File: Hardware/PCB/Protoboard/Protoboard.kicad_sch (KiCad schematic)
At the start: 17 parts, among them J1 Conn_01x05_Female, J2 Conn_01x08_Female, J3 Conn_01x08_Female, U1 MAX6971ANG_

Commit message: Protoboard layout.
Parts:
- R5, R6, R7, R8: value 10 -> 100
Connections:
- net LATCH: now also R1.2; no longer R2.2
- net SCK: now also R2.2; no longer R1.2
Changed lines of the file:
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@@
   (junction (at 165.1 53.34) (diameter 0) (color 0 0 0 0)
   )
-  (junction (at 140.97 26.035) (diameter 0) (color 0 0 0 0)
+  (junction (at 141.605 26.035) (diameter 0) (color 0 0 0 0)
   )
   (junction (at 161.29 50.8) (diameter 0) (color 0 0 0 0)
@@
   )
   (no_connect (at 110.49 45.72))
-  (wire (pts (xy 140.97 22.225) (xy 140.97 26.035))
+  (wire (pts (xy 141.605 22.225) (xy 141.605 26.035))
     (stroke (width 0) (type default) (color 0 0 0 0))
   )
@@
     (stroke (width 0) (type default) (color 0 0 0 0))
   )
+  (wire (pts (xy 142.24 88.9) (xy 140.97 88.9))
+    (stroke (width 0) (type default) (color 0 0 0 0))
+  )
   (wire (pts (xy 153.67 30.48) (xy 157.48 30.48))
     (stroke (width 0) (type default) (color 0 0 0 0))
@@
     (stroke (width 0) (type default) (color 0 0 0 0))
   )
-  (wire (pts (xy 140.97 26.035) (xy 140.97 35.56))
+  (wire (pts (xy 141.605 26.035) (xy 141.605 35.56))
     (stroke (width 0) (type default) (color 0 0 0 0))
   )
@@
     (stroke (width 0) (type default) (color 0 0 0 0))
   )
+  (wire (pts (xy 141.605 26.035) (xy 140.97 26.035))
+    (stroke (width 0) (type default) (color 0 0 0 0))
+  )
   (wire (pts (xy 151.13 66.04) (xy 140.97 66.04))
     (stroke (width 0) (type default) (color 0 0 0 0))
@@
     (stroke (width 0) (type default) (color 0 0 0 0))
   )
+  (wire (pts (xy 141.605 35.56) (xy 140.97 35.56))
+    (stroke (width 0) (type default) (color 0 0 0 0))
+  )
   (wire (pts (xy 168.91 55.88) (xy 140.97 55.88))
     (stroke (width 0) (type default) (color 0 0 0 0))
@@
     (effects (font (size 1.27 1.27)) (justify left bottom))
   )
-  (label "LATCH" (at 55.88 43.18 0)
-    (effects (font (size 1.27 1.27)) (justify left bottom))
-  )
-  (label "SPI1_MOSI" (at 55.88 40.64 0)
-    (effects (font (size 1.27 1.27)) (justify left bottom))
-  )
-  (label "SPI1_5V" (at 55.88 38.1 0)
-    (effects (font (size 1.27 1.27)) (justify left bottom))
-  )
-  (label "SPI1_GND" (at 55.88 48.26 0)
-    (effects (font (size 1.27 1.27)) (justify left bottom))
-  )
-  (label "SPI1_SCK" (at 59.055 45.72 0)
-    (effects (font (size 1.27 1.27)) (justify left bottom))
-  )
-  (global_label "SCK" (shape input) (at 73.66 45.72 0) (fields_autoplaced)
-    (effects (font (size 1.27 1.27)) (justify left))
-    (property "Intersheet References" "${INTERSHEET_REFS}" (id 0) (at 79.8226 45.6406 0)
+  (label "SCK" (at 55.88 43.18 0)
+    (effects (font (size 1.27 1.27)) (justify left bottom))
+  )
+  (label "MOSI" (at 55.88 40.64 0)
+    (effects (font (size 1.27 1.27)) (justify left bottom))
+  )
+  (label "VCC" (at 55.88 38.1 0)
+    (effects (font (size 1.27 1.27)) (justify left bottom))
+  )
+  (label "GND" (at 55.88 48.26 0)
+    (effects (font (size 1.27 1.27)) (justify left bottom))
+  )
+  (label "LATCH" (at 59.055 45.72 0)
+    (effects (font (size 1.27 1.27)) (justify left bottom))
+  )
+  (global_label "LATCH" (shape input) (at 73.66 45.72 0) (fields_autoplaced)
+    (effects (font (size 1.27 1.27)) (justify left))
+    (property "Intersheet References" "${INTERSHEET_REFS}" (id 0) (at 81.7579 45.6406 0)
       (effects (font (size 1.27 1.27)) (justify left) hide)
     )
@@
     )
   )
-  (global_label "LATCH" (shape input) (at 67.31 43.18 0) (fields_autoplaced)
-    (effects (font (size 1.27 1.27)) (justify left))
-    (property "Intersheet References" "${INTERSHEET_REFS}" (id 0) (at 75.4079 43.1006 0)
+  (global_label "SCK" (shape input) (at 67.31 43.18 0) (fields_autoplaced)
+    (effects (font (size 1.27 1.27)) (justify left))
+    (property "Intersheet References" "${INTERSHEET_REFS}" (id 0) (at 73.4726 43.1006 0)
       (effects (font (size 1.27 1.27)) (justify left) hide)
     )
@@
     )
   )
-  (global_label "GND" (shape input) (at 140.97 88.9 0) (fields_autoplaced)
-    (effects (font (size 1.27 1.27)) (justify left))
-    (property "Intersheet References" "${INTERSHEET_REFS}" (id 0) (at 147.2536 88.8206 0)
+  (global_label "GND" (shape input) (at 142.24 88.9 0) (fields_autoplaced)
+    (effects (font (size 1.27 1.27)) (justify left))
+    (property "Intersheet References" "${INTERSHEET_REFS}" (id 0) (at 148.5236 88.8206 0)
       (effects (font (size 1.27 1.27)) (justify left) hide)
     )
@@
     )
   )
-  (global_label "VCC" (shape input) (at 140.97 22.225 90) (fields_autoplaced)
-    (effects (font (size 1.27 1.27)) (justify left))
-    (property "Intersheet References" "${INTERSHEET_REFS}" (id 0) (at 140.8906 16.1833 90)
+  (global_label "VCC" (shape input) (at 141.605 22.225 90) (fields_autoplaced)
+    (effects (font (size 1.27 1.27)) (justify left))
+    (property "Intersheet References" "${INTERSHEET_REFS}" (id 0) (at 141.5256 16.1833 90)
       (effects (font (size 1.27 1.27)) (justify left) hide)
     )
@@
       (effects (font (size 1.27 1.27)) (justify left))
     )
-    (property "Value" "10" (id 1) (at 152.4 29.21 0)
+    (property "Value" "100" (id 1) (at 152.4 29.21 0)
       (effects (font (size 1.27 1.27)) (justify left))
     )
@@
       (effects (font (size 1.27 1.27)) (justify left))
     )
-    (property "Value" "10" (id 1) (at 148.59 29.21 0)
+    (property "Value" "100" (id 1) (at 148.59 29.21 0)
       (effects (font (size 1.27 1.27)) (justify left))
     )
@@
       (effects (font (size 1.27 1.27)) (justify left))
     )
-    (property "Value" "10" (id 1) (at 156.21 29.21 0)
+    (property "Value" "100" (id 1) (at 156.21 29.21 0)
       (effects (font (size 1.27 1.27)) (justify left))
     )
@@
       (effects (font (size 1.27 1.27)) (justify left))
     )
-    (property "Value" "10" (id 1) (at 144.78 29.21 0)
+    (property "Value" "100" (id 1) (at 144.78 29.21 0)
       (effects (font (size 1.27 1.27)) (justify left))
     )
@@
     )
     (path "/de5ce3a4-6348-4028-bcbc-796d25ddc390"
-      (reference "R5") (unit 1) (value "10") (footprint "Resistor_SMD:R_0805_2012Metric_Pad1.20x1.40mm_HandSolder")
+      (reference "R5") (unit 1) (value "100") (footprint "Resistor_SMD:R_0805_2012Metric_Pad1.20x1.40mm_HandSolder")
     )
     (path "/2f1e73e5-ba84-4857-a21b-a2e8a5ea274f"
-      (reference "R6") (unit 1) (value "10") (footprint "Resistor_SMD:R_0805_2012Metric_Pad1.20x1.40mm_HandSolder")
+      (reference "R6") (unit 1) (value "100") (footprint "Resistor_SMD:R_0805_2012Metric_Pad1.20x1.40mm_HandSolder")
     )
     (path "/10f6fcf9-ce65-45e1-81f4-5a5c35568bfc"
-      (reference "R7") (unit 1) (value "10") (footprint "Resistor_SMD:R_0805_2012Metric_Pad1.20x1.40mm_HandSolder")
+      (reference "R7") (unit 1) (value "100") (footprint "Resistor_SMD:R_0805_2012Metric_Pad1.20x1.40mm_HandSolder")
     )
     (path "/60a63df7-538f-43ef-b8d3-5286e6518d70"
-      (reference "R8") (unit 1) (value "10") (footprint "Resistor_SMD:R_0805_2012Metric_Pad1.20x1.40mm_HandSolder")
+      (reference "R8") (unit 1) (value "100") (footprint "Resistor_SMD:R_0805_2012Metric_Pad1.20x1.40mm_HandSolder")
     )
     (path "/3de5d5fd-cc44-4147-a2dc-e5797db63fd1"

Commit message: Finished Protoboard
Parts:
- added H1, H2, H3, H4: MountingHole, MountingHole:MountingHole_2.2mm_M2, symbol Mechanical:MountingHole
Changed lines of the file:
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@@
+    )
+  )
+  (symbol (lib_id "Mechanical:MountingHole") (at 37.465 72.39 0) (unit 1)
+    (in_bom yes) (on_board yes) (fields_autoplaced)
+    (property "Reference" "H3" (id 0) (at 40.64 71.1199 0)
+      (effects (font (size 1.27 1.27)) (justify left))
+    )
+    (property "Value" "MountingHole" (id 1) (at 40.64 73.6599 0)
+      (effects (font (size 1.27 1.27)) (justify left))
+    )
+    (property "Footprint" "MountingHole:MountingHole_2.2mm_M2" (id 2) (at 37.465 72.39 0)
+      (effects (font (size 1.27 1.27)) hide)
+    )
+    (property "Datasheet" "~" (id 3) (at 37.465 72.39 0)
+      (effects (font (size 1.27 1.27)) hide)
     )
   )
@@
     (pin "1")
     (pin "2")
+  )
+  (symbol (lib_id "Mechanical:MountingHole") (at 37.465 77.47 0) (unit 1)
+    (in_bom yes) (on_board yes) (fields_autoplaced)
+    (property "Reference" "H4" (id 0) (at 40.64 76.1999 0)
+      (effects (font (size 1.27 1.27)) (justify left))
+    )
+    (property "Value" "MountingHole" (id 1) (at 40.64 78.7399 0)
+      (effects (font (size 1.27 1.27)) (justify left))
+    )
+    (property "Footprint" "MountingHole:MountingHole_2.2mm_M2" (id 2) (at 37.465 77.47 0)
+      (effects (font (size 1.27 1.27)) hide)
+    )
+    (property "Datasheet" "~" (id 3) (at 37.465 77.47 0)
+      (effects (font (size 1.27 1.27)) hide)
+    )
+  )
+  (symbol (lib_id "Mechanical:MountingHole") (at 37.465 67.31 0) (unit 1)
+    (in_bom yes) (on_board yes) (fields_autoplaced)
+    (property "Reference" "H2" (id 0) (at 40.64 66.0399 0)
+      (effects (font (size 1.27 1.27)) (justify left))
+    )
+    (property "Value" "MountingHole" (id 1) (at 40.64 68.5799 0)
+      (effects (font (size 1.27 1.27)) (justify left))
+    )
+    (property "Footprint" "MountingHole:MountingHole_2.2mm_M2" (id 2) (at 37.465 67.31 0)
+      (effects (font (size 1.27 1.27)) hide)
+    )
+    (property "Datasheet" "~" (id 3) (at 37.465 67.31 0)
+      (effects (font (size 1.27 1.27)) hide)
+    )
   )
   (symbol (lib_id "Device:C") (at 137.16 26.035 90) (unit 1)
@@
     (pin "9")
   )
+  (symbol (lib_id "Mechanical:MountingHole") (at 37.465 62.23 0) (unit 1)
+    (in_bom yes) (on_board yes) (fields_autoplaced)
+    (property "Reference" "H1" (id 0) (at 40.64 60.9599 0)
+      (effects (font (size 1.27 1.27)) (justify left))
+    )
+    (property "Value" "MountingHole" (id 1) (at 40.64 63.4999 0)
+      (effects (font (size 1.27 1.27)) (justify left))
+    )
+    (property "Footprint" "MountingHole:MountingHole_2.2mm_M2" (id 2) (at 37.465 62.23 0)
+      (effects (font (size 1.27 1.27)) hide)
+    )
+    (property "Datasheet" "~" (id 3) (at 37.465 62.23 0)
+      (effects (font (size 1.27 1.27)) hide)
+    )
+  )
   (symbol (lib_id "Device:R") (at 146.05 34.29 0) (unit 1)
     (in_bom yes) (on_board yes)
@@
       (reference "C1") (unit 1) (value "0.1uf") (footprint "Capacitor_SMD:C_0805_2012Metric_Pad1.18x1.45mm_HandSolder")
     )
+    (path "/bfdbfa5d-af60-4bcb-aaee-563dc6121e2f"
+      (reference "H1") (unit 1) (value "MountingHole") (footprint "MountingHole:MountingHole_2.2mm_M2")
+    )
+    (path "/6a9026f4-97ad-4ca6-b8a7-4b78e7eaa11b"
+      (reference "H2") (unit 1) (value "MountingHole") (footprint "MountingHole:MountingHole_2.2mm_M2")
+    )
+    (path "/0d0a8cf0-7e30-4463-a75a-b09ac9dce329"
+      (reference "H3") (unit 1) (value "MountingHole") (footprint "MountingHole:MountingHole_2.2mm_M2")
+    )
+    (path "/683869c3-2652-4a1a-8cb4-4298fc933778"
+      (reference "H4") (unit 1) (value "MountingHole") (footprint "MountingHole:MountingHole_2.2mm_M2")
+    )
     (path "/61c1ad0a-88fa-4e84-b6d4-f39d3cd9072a"

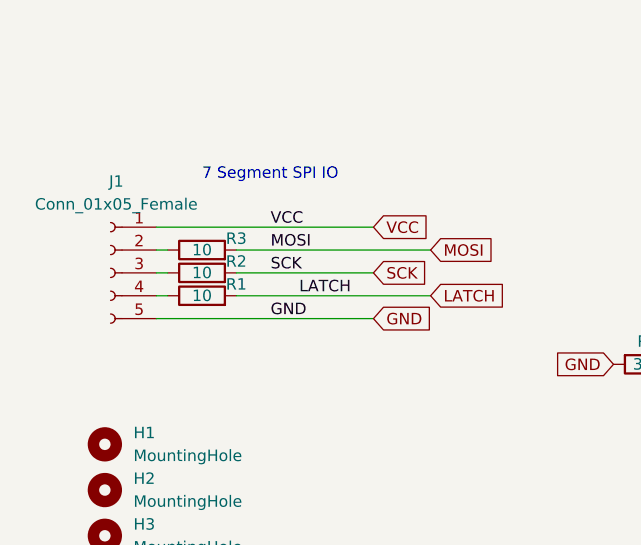
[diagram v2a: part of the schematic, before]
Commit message: Fixed Silkscreen
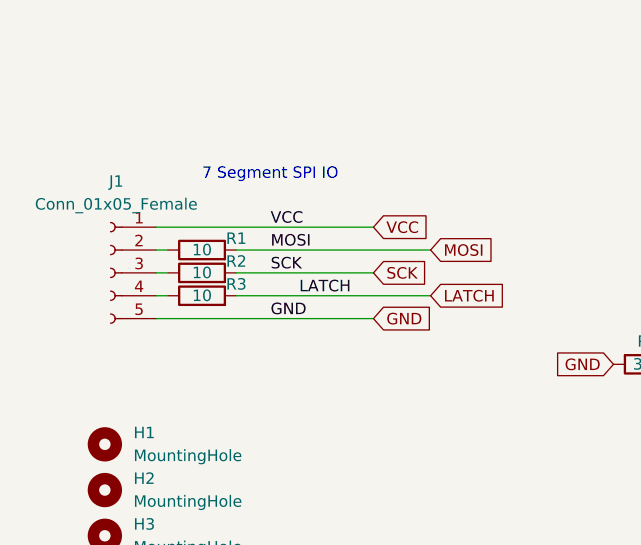
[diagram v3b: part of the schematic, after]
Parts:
- renumbered R3 to R1, R1 to R3
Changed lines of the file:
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@@
   (symbol (lib_id "Device:R") (at 48.26 45.72 90) (unit 1)
     (in_bom yes) (on_board yes)
-    (property "Reference" "R1" (id 0) (at 52.07 44.45 90))
+    (property "Reference" "R3" (id 0) (at 52.07 44.45 90))
     (property "Value" "10" (id 1) (at 48.26 45.72 90))
     (property "Footprint" "Resistor_SMD:R_0805_2012Metric_Pad1.20x1.40mm_HandSolder" (id 2) (at 48.26 47.498 90)
@@
   (symbol (lib_id "Device:R") (at 48.26 40.64 90) (unit 1)
     (in_bom yes) (on_board yes)
-    (property "Reference" "R3" (id 0) (at 52.07 39.37 90))
+    (property "Reference" "R1" (id 0) (at 52.07 39.37 90))
     (property "Value" "10" (id 1) (at 48.26 40.64 90))
     (property "Footprint" "Resistor_SMD:R_0805_2012Metric_Pad1.20x1.40mm_HandSolder" (id 2) (at 48.26 42.418 90)
@@
       (reference "J3") (unit 1) (value "Conn_01x08_Female") (footprint "Connector_PinSocket_2.54mm:PinSocket_1x08_P2.54mm_Vertical")
     )
-    (path "/8277476c-b798-4057-b547-52abc06333bd"
+    (path "/ad10a4b7-2487-448c-860c-e5fa438bed4f"
       (reference "R1") (unit 1) (value "10") (footprint "Resistor_SMD:R_0805_2012Metric_Pad1.20x1.40mm_HandSolder")
     )
@@
       (reference "R2") (unit 1) (value "10") (footprint "Resistor_SMD:R_0805_2012Metric_Pad1.20x1.40mm_HandSolder")
     )
-    (path "/ad10a4b7-2487-448c-860c-e5fa438bed4f"
+    (path "/8277476c-b798-4057-b547-52abc06333bd"
       (reference "R3") (unit 1) (value "10") (footprint "Resistor_SMD:R_0805_2012Metric_Pad1.20x1.40mm_HandSolder")
     )
